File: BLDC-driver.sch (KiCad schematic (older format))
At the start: 9 parts, among them Q1 IPD50R380CE, Q2 IPD50R380CE, U1 NCP81151

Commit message: annotate
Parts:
- gave numbers to parts that had none: 5
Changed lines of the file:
@@
 	8650 3050 8650 2900
 $Comp
-L power:+5V #PWR?
+L power:+5V #PWR0104
 U 1 1 5EE8B1BC
 P 6850 1800
-F 0 "#PWR?" H 6850 1650 50  0001 C CNN
+F 0 "#PWR0104" H 6850 1650 50  0001 C CNN
 F 1 "+5V" H 6865 1973 50  0000 C CNN
 F 2 "" H 6850 1800 50  0001 C CNN
@@
 	6850 2000 7000 2000
 $Comp
-L Device:C_Small C?
+L Device:C_Small C2
 U 1 1 5EE8BA1A
 P 9000 1500
-F 0 "C?" H 9200 1550 50  0000 R CNN
+F 0 "C2" H 9200 1550 50  0000 R CNN
 F 1 "4.7uF" H 9200 1400 50  0000 R CNN
 F 2 "Capacitor_SMD:C_0603_1608Metric" H 9000 1500 50  0001 C CNN
@@
 $EndComp
 $Comp
-L power:GND #PWR?
+L power:GND #PWR0105
 U 1 1 5EE8C1E2
 P 9000 1600
-F 0 "#PWR?" H 9000 1350 50  0001 C CNN
+F 0 "#PWR0105" H 9000 1350 50  0001 C CNN
 F 1 "GND" H 9005 1427 50  0000 C CNN
 F 2 "" H 9000 1600 50  0001 C CNN
@@
 Connection ~ 8650 1400
 $Comp
-L Device:C_Small C?
+L Device:C_Small C3
 U 1 1 5EE8CF8E
 P 9200 1500
-F 0 "C?" H 9108 1546 50  0000 R CNN
+F 0 "C3" H 9108 1546 50  0000 R CNN
 F 1 "4.7uF" H 9108 1455 50  0000 R CNN
 F 2 "Capacitor_SMD:C_0603_1608Metric" H 9200 1500 50  0001 C CNN
@@
 $EndComp
 $Comp
-L power:GND #PWR?
+L power:GND #PWR0106
 U 1 1 5EE8D549
 P 9200 1600
-F 0 "#PWR?" H 9200 1350 50  0001 C CNN
+F 0 "#PWR0106" H 9200 1350 50  0001 C CNN
 F 1 "GND" H 9205 1427 50  0000 C CNN
 F 2 "" H 9200 1600 50  0001 C CNN
@@
 PH_A
 $Comp
-L Device:C_Small C?
+L Device:C_Small C4
 U 1 1 5EE8DE22
 P 6700 2000
-F 0 "C?" V 6800 2100 50  0000 R CNN
+F 0 "C4" V 6800 2100 50  0000 R CNN
 F 1 "4.7uF" V 6800 1950 50  0000 R CNN
 F 2 "Capacitor_SMD:C_0603_1608Metric" H 6700 2000 50  0001 C CNN
@@
 Connection ~ 6850 2000
 $Comp
-L power:GND #PWR?
+L power:GND #PWR0107
 U 1 1 5EE8F89C
 P 6550 2000
-F 0 "#PWR?" H 6550 1750 50  0001 C CNN
+F 0 "#PWR0107" H 6550 1750 50  0001 C CNN
 F 1 "GND" H 6555 1827 50  0000 C CNN
 F 2 "" H 6550 2000 50  0001 C CNN
@@
 	6550 2000 6600 2000
 $Comp
-L Transistor_FET:IPD50R380CE Q?
+L Transistor_FET:IPD50R380CE Q3
 U 1 1 5EE928AB
 P 9250 2100
-F 0 "Q?" H 9455 2131 50  0000 L CNN
+F 0 "Q3" H 9455 2131 50  0000 L CNN
 F 1 "IPD50R380CE" H 9455 2054 31  0000 L CNN
 F 2 "Package_TO_SOT_SMD:TO-252-2" H 9450 2025 50  0001 L CIN
@@
 Connection ~ 8350 2100
 $Comp
-L Transistor_FET:IPD50R380CE Q?
+L Transistor_FET:IPD50R380CE Q4
 U 1 1 5EE9355C
 P 9250 2700
-F 0 "Q?" H 9455 2731 50  0000 L CNN
+F 0 "Q4" H 9455 2731 50  0000 L CNN
 F 1 "IPD50R380CE" H 9455 2654 31  0000 L CNN
 F 2 "Package_TO_SOT_SMD:TO-252-2" H 9450 2625 50  0001 L CIN
@@
 Connection ~ 9350 2400
 $Comp
-L power:GND #PWR?
+L power:GND #PWR0108
 U 1 1 5EE9496B
 P 9350 3050
-F 0 "#PWR?" H 9350 2800 50  0001 C CNN
+F 0 "#PWR0108" H 9350 2800 50  0001 C CNN
 F 1 "GND" H 9355 2877 50  0000 C CNN
 F 2 "" H 9350 3050 50  0001 C CNN

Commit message: Schematic progress
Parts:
- removed Q1, Q2, Q3, Q4: IPD50R380CE, Package_TO_SOT_SMD:TO-252-2, symbol Transistor_FET:IPD50R380CE
- added C10, C6: 100nF, Capacitor_SMD:C_0603_1608Metric, symbol Device:C_Small
- added C11, C12, C5, C7, C8, C9: 4.7uF, Capacitor_SMD:C_0603_1608Metric, symbol Device:C_Small
- added Q1, Q2, Q3, Q4, Q5, Q6: FDMS86550, Package_TO_SOT_SMD:TDSON-8-1, symbol Transistor_FET:FDMS86550
- added U2, U3: NCP81151, Package_DFN_QFN:DFN-8-1EP_2x2mm_P0.5mm_EP0.9x1.3mm, symbol BLDC-driver-rescue:NCP81151-userdvc
- added U4: LPC1112FHN33-101, Package_DFN_QFN:QFN-32-1EP_7x7mm_P0.65mm_EP4.7x4.7mm, symbol MCU_NXP_LPC:LPC1112FHN33-101
- U1: symbol userdvc:NCP81151 -> BLDC-driver-rescue:NCP81151-userdvc
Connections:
- net labels added: +3.3V, HG_A, HG_B, HG_C, LG_A, LG_B, LG_C, PH_B, PH_C
- wire segments 35 -> 73
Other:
- moved on the sheet: C1, C2, C3, C4

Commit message: Latest
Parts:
- added C13, C14, C15: 2.7nF, Capacitor_SMD:C_0603_1608Metric, symbol Device:C_Small
- added C16, C17, C18: 4.7uF, Capacitor_SMD:C_1206_3216Metric, symbol Device:C_Small
- added R1, R2, R3: 2.2, Resistor_SMD:R_0603_1608Metric, symbol Device:R_Small
- added R4: 10k, Resistor_SMD:R_0603_1608Metric, symbol Device:R_Small
- added TH1: 10k, Resistor_SMD:R_0603_1608Metric, symbol Device:Thermistor_NTC
- added U5: AS5600, Package_SO:SOIC-8_3.9x4.9mm_P1.27mm, symbol BLDC-driver-rescue:AS5600
- C11, C12, C2, C3, C7, C8: footprint Capacitor_SMD:C_0603_1608Metric -> Capacitor_SMD:C_1206_3216Metric
- U1, U2, U3: footprint Package_DFN_QFN:DFN-8-1EP_2x2mm_P0.5mm_EP0.9x1.3mm -> Package_DFN_QFN:DFN-8-1EP_2x2mm_P0.5mm_EP0.9x1.5mm
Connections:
- net +24V: now also C16.1, C17.1, C18.1
- net +3V3: now also TH1.1
- net +5V: now also U1.3 (EN), U2.3 (EN), U3.3 (EN)
- net GND: now also C13.2, C14.2, C15.2, C16.2, C17.2, C18.2, R4.2, U5.4 (GND)
- net PH_A: now also R1.1
- net PH_B: now also R2.1
- net PH_C: now also R3.1
- net PWM_A: now reaches U1.2 (PWM)
- net PWM_A: now also U4.19 (PIO0_10)
- net PWM_B: now reaches U3.2 (PWM)
- net PWM_B: now also U4.21 (PIO0_11)
- net PWM_C: now reaches U2.2 (PWM)
- net PWM_C: now also U4.18 (PIO0_9)
- net ENBL: now reaches U4.17 (PIO0_8)
- new net: C13.1, R1.2
- new net: C14.1, R2.2
- new net: C15.1, R3.2
- new net FET_TEMP: R4.1, TH1.2

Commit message: Latest
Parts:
- added C19, C20: 100nF, Capacitor_SMD:C_0603_1608Metric, symbol Device:C_Small
- added J1: Conn_01x06, Connector_PinHeader_2.54mm:PinHeader_1x08_P2.54mm_Vertical, symbol Connector_Generic:Conn_01x08
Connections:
- net +3V3: now also U5.1 (VDD5V), U5.2 (VDD3V3), C20.2
- net FET_TEMP: now also U4.20 (PIO1_10), C19.2
- net GND: now also C19.1, C20.1, J1.1 (Pin_1)
- net PWM_A: now also U4.26 (PIO1_4); no longer U4.19 (PIO0_10)
- net PWM_B: now also U4.24 (PIO1_2); no longer U4.21 (PIO0_11)
- net PWM_C: now also U4.23 (PIO1_1); no longer U4.18 (PIO0_9)
- net SCL: now reaches U4.10 (PIO0_4)
- net SCL: now also U5.7 (SCL), J1.5 (Pin_5)
- net SDA: now reaches U4.11 (PIO0_5)
- net SDA: now also U5.6 (SDA), J1.6 (Pin_6)
- net SWDIO: now reaches U4.25 (PIO1_3)
- net SWDIO: now also J1.4 (Pin_4)
- net RXD: now reaches U4.31 (PIO1_6)
- net RXD: now also J1.8 (Pin_8)
- net TXD: now reaches U4.32 (PIO1_7)
- net TXD: now also J1.7 (Pin_7)
- net ENBL: no longer names the net of U4.17 (PIO0_8)
- new net SWCLK: J1.3 (Pin_3), U4.19 (PIO0_10)
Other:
- note added: "CT32B1_MAT0"
- note added: "CT32B1_MAT1"
- note added: "CT32B1_MAT3"
- moved on the sheet: U5
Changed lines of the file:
@@
 P 3300 3150
 F 0 "U4" H 3300 3000 50  0000 C CNN
-F 1 "LPC1112FHN33-101" H 3200 2650 50  0000 C CNN
+F 1 "LPC1112FHN33-101" H 3150 2700 50  0000 C CNN
 F 2 "Package_DFN_QFN:QFN-32-1EP_7x7mm_P0.65mm_EP4.7x4.7mm" H 4400 4250 50  0001 C CNN
 F 3 "https://www.nxp.com/documents/data_sheet/LPC111X.pdf" H 3300 3150 50  0001 C CNN
@@
 L BLDC-driver-rescue:AS5600 U5
 U 1 1 5EFF18B3
-P 5450 3200
-F 0 "U5" H 5625 3365 50  0000 C CNN
-F 1 "AS5600" H 5625 3274 50  0000 C CNN
-F 2 "Package_SO:SOIC-8_3.9x4.9mm_P1.27mm" H 5450 3200 50  0001 C CNN
-F 3 "" H 5450 3200 50  0001 C CNN
-	1    5450 3200
+P 6250 3250
+F 0 "U5" H 6425 3415 50  0000 C CNN
+F 1 "AS5600" H 6425 3324 50  0000 C CNN
+F 2 "Package_SO:SOIC-8_3.9x4.9mm_P1.27mm" H 6250 3250 50  0001 C CNN
+F 3 "" H 6250 3250 50  0001 C CNN
+	1    6250 3250
 	1    0    0    -1
 $EndComp
@@
 L power:GND #PWR0130
 U 1 1 5EFF1DB5
-P 5100 3600
-F 0 "#PWR0130" H 5100 3350 50  0001 C CNN
-F 1 "GND" H 5105 3427 50  0000 C CNN
-F 2 "" H 5100 3600 50  0001 C CNN
-F 3 "" H 5100 3600 50  0001 C CNN
-	1    5100 3600
-	1    0    0    -1
-$EndComp
-Text Label 2600 3250 2    50   ~ 0
+P 5900 3650
+F 0 "#PWR0130" H 5900 3400 50  0001 C CNN
+F 1 "GND" H 5905 3477 50  0000 C CNN
+F 2 "" H 5900 3650 50  0001 C CNN
+F 3 "" H 5900 3650 50  0001 C CNN
+	1    5900 3650
+	1    0    0    -1
+$EndComp
+Text Label 4200 2450 0    50   ~ 0
 PWM_C
-Text Label 2600 3350 2    50   ~ 0
+Text Label 4200 2750 0    50   ~ 0
 PWM_A
-Text Label 2600 3450 2    50   ~ 0
+Text Label 4200 2550 0    50   ~ 0
 PWM_B
-Text Label 2600 3150 2    50   ~ 0
-ENBL
 $Comp
 L power:+5V #PWR0131
@@
 L power:GND #PWR0134
 U 1 1 5F0691FC
-P 5900 1900
-F 0 "#PWR0134" H 5900 1650 50  0001 C CNN
-F 1 "GND" H 5905 1727 50  0000 C CNN
-F 2 "" H 5900 1900 50  0001 C CNN
-F 3 "" H 5900 1900 50  0001 C CNN
-	1    5900 1900
+P 5900 2000
+F 0 "#PWR0134" H 5900 1750 50  0001 C CNN
+F 1 "GND" H 5905 1827 50  0000 C CNN
+F 2 "" H 5900 2000 50  0001 C CNN
+F 3 "" H 5900 2000 50  0001 C CNN
+	1    5900 2000
 	1    0    0    -1
 $EndComp
@@
 	1    0    0    -1
 $EndComp
-Text Label 6100 1600 0    50   ~ 0
+Text Label 6650 1600 0    50   ~ 0
 FET_TEMP
-Wire Wire Line
-	6100 1600 5900 1600
 Connection ~ 5900 1600
 Wire Wire Line
 	5900 1600 5900 1500
+Text Label 2400 2750 2    50   ~ 0
+SCL
+Text Label 2400 2850 2    50   ~ 0
+SDA
+Wire Wire Line
+	2400 2850 2600 2850
+Wire Wire Line
+	2600 2750 2400 2750
+Text Label 2400 3350 2    50   ~ 0
+SWCLK
+Text Label 4200 2650 0    50   ~ 0
+SWDIO
+Wire Wire Line
+	4200 2650 4000 2650
+Wire Wire Line
+	2600 3350 2400 3350
+Text Label 4200 2950 0    50   ~ 0
+RXD
+Text Label 4200 3050 0    50   ~ 0
+TXD
+Wire Wire Line
+	4200 3050 4000 3050
+Wire Wire Line
+	4000 2950 4200 2950
+Wire Wire Line
+	4200 2450 4000 2450
+Wire Wire Line
+	4000 2550 4200 2550
+Wire Wire Line
+	4000 2750 4200 2750
+Text Notes 4550 2750 0    50   ~ 0
+CT32B1_MAT3
+Text Notes 4550 2550 0    50   ~ 0
+CT32B1_MAT1
+Text Notes 4550 2450 0    50   ~ 0
+CT32B1_MAT0
+$Comp
+L power:+3.3V #PWR0136
+U 1 1 5F0C7A64
+P 5700 3250
+F 0 "#PWR0136" H 5700 3100 50  0001 C CNN
+F 1 "+3.3V" H 5715 3423 50  0000 C CNN
+F 2 "" H 5700 3250 50  0001 C CNN
+F 3 "" H 5700 3250 50  0001 C CNN
+	1    5700 3250
+	1    0    0    -1
+$EndComp
+Wire Wire Line
+	5700 3250 5700 3350
+Wire Wire Line
+	5700 3450 5900 3450
+Wire Wire Line
+	5900 3350 5700 3350
+Connection ~ 5700 3350
+Wire Wire Line
+	5700 3350 5700 3450
+$Comp
+L Device:C_Small C20
+U 1 1 5F0CF40D
+P 5500 3550
+F 0 "C20" V 5271 3550 50  0000 C CNN
+F 1 "100nF" V 5362 3550 50  0000 C CNN
+F 2 "Capacitor_SMD:C_0603_1608Metric" H 5500 3550 50  0001 C CNN
+F 3 "~" H 5500 3550 50  0001 C CNN
+	1    5500 3550
+	-1   0    0    1
+$EndComp
+Wire Wire Line
+	5500 3450 5700 3450
+Connection ~ 5700 3450
+Wire Wire Line
+	5500 3650 5900 3650
+Connection ~ 5900 3650
+Text Label 7150 3450 0    50   ~ 0
+SCL
+Text Label 7150 3550 0    50   ~ 0
+SDA
+Wire Wire Line
+	7150 3550 6950 3550
+Wire Wire Line
+	6950 3450 7150 3450
+$Comp
+L Device:C_Small C19
+U 1 1 5F0DE4B5
+P 6250 1750
+F 0 "C19" V 6021 1750 50  0000 C CNN
+F 1 "100nF" V 6112 1750 50  0000 C CNN
+F 2 "Capacitor_SMD:C_0603_1608Metric" H 6250 1750 50  0001 C CNN
+F 3 "~" H 6250 1750 50  0001 C CNN
+	1    6250 1750
+	-1   0    0    1
+$EndComp
+Wire Wire Line
+	5900 1600 6250 1600
+Wire Wire Line
+	6250 1650 6250 1600
+Connection ~ 6250 1600
+Wire Wire Line
+	6250 1600 6650 1600
+Wire Wire Line
+	5900 2000 5900 1950
+Wire Wire Line
+	5900 1950 6250 1950
+Wire Wire Line
+	6250 1950 6250 1850
+Connection ~ 5900 1950
+Wire Wire Line
+	5900 1950 5900 1900
+Text Label 4200 3350 0    50   ~ 0
+FET_TEMP
+Wire Wire Line
+	4000 3350 4200 3350
+$Comp
+L Connector_Generic:Conn_01x08 J1
+U 1 1 5F108F52
+P 1250 5800
+F 0 "J1" H 1168 5175 50  0000 C CNN
+F 1 "Conn_01x06" H 1168 5266 50  0000 C CNN
+F 2 "Connector_PinHeader_2.54mm:PinHeader_1x08_P2.54mm_Vertical" H 1250 5800 50  0001 C CNN
+F 3 "~" H 1250 5800 50  0001 C CNN
+	1    1250 5800
+	-1   0    0    1
+$EndComp
+Text Label 1650 5400 0    50   ~ 0
+RXD
+Text Label 1650 5500 0    50   ~ 0
+TXD
+Wire Wire Line
+	1650 5500 1450 5500
+Wire Wire Line
+	1450 5400 1650 5400
+Text Label 1650 5700 0    50   ~ 0
+SCL
+Text Label 1650 5600 0    50   ~ 0
+SDA
+Wire Wire Line
+	1650 5600 1450 5600
+Wire Wire Line
+	1450 5700 1650 5700
+Text Label 1650 5900 0    50   ~ 0
+SWCLK
+Text Label 1650 5800 0    50   ~ 0
+SWDIO
+Wire Wire Line
+	1650 5800 1450 5800
+Wire Wire Line
+	1450 5900 1650 5900
+$Comp
+L power:GND #PWR0137
+U 1 1 5F120A4B
+P 1450 6100
+F 0 "#PWR0137" H 1450 5850 50  0001 C CNN
+F 1 "GND" H 1455 5927 50  0000 C CNN
+F 2 "" H 1450 6100 50  0001 C CNN
+F 3 "" H 1450 6100 50  0001 C CNN
+	1    1450 6100
+	1    0    0    -1
+$EndComp
 $EndSCHEMATC

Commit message: Latest
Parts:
- added C23: 10nF, Capacitor_SMD:C_0603_1608Metric, symbol Device:C_Small
- added C24, C25, C26: 1uF, Capacitor_SMD:C_0603_1608Metric, symbol Device:C_Small
- added C5, C6: 100nF, Capacitor_SMD:C_0603_1608Metric, symbol Device:C_Small
- added D1: 30V, Diode_SMD:D_SOD-323, symbol Device:D_Schottky_Small
- added JP1: BOOT, Jumper:SolderJumper-2_P1.3mm_Open_Pad1.0x1.5mm, symbol Device:Jumper
- added L1: 4.7uH, Inductor_SMD:L_Taiyo-Yuden_MD-3030, symbol Device:L_Small
- added NT1: Net-Tie_2, NetTie:NetTie-2_SMD_Pad0.5mm, symbol Device:Net-Tie_2
- added R2, R3: 10k, Resistor_SMD:R_0603_1608Metric, symbol Device:R_Small
- added R7: 100k, Resistor_SMD:R_0603_1608Metric, symbol Device:R_Small
- added R8: 47k, Resistor_SMD:R_0603_1608Metric, symbol Device:R_Small
- added R9: 9.1k, Resistor_SMD:R_0603_1608Metric, symbol Device:R_Small
- added U6: MP2359, Package_TO_SOT_SMD:SOT-23-6, symbol BLDC-driver-rescue:MP2359
- added U7: MIC5504-3.3YM5, Package_TO_SOT_SMD:SOT-23-5, symbol Regulator_Linear:MIC5504-3.3YM5
- J1: footprint Connector_PinHeader_2.54mm:PinHeader_1x08_P2.54mm_Vertical -> Connector_PinHeader_2.00mm:PinHeader_1x08_P2.00mm_Vertical
- U1: value NCP81151 -> ADP3120A
- U4: renamed from U3; value NCP81151 -> ADP3120A
- U5: renamed from U2; value NCP81151 -> ADP3120A
- renumbered C2 to C1, C7 to C10, C8 to C11, C17 to C12, C10 to C13, C9 to C14, C11 to C15, C12 to C16, C18 to C17, C6 to C18, C5 to C19, C3 to C2, C13 to C20, C14 to C21, C15 to C22, C16 to C3, C19 to C4, C1 to C7, C4 to C8, C20 to C9, TH1 to NTC1, Q3 to Q1, Q4 to Q2, Q5 to Q3, Q6 to Q4, Q1 to Q5, Q2 to Q6, R4 to R1, R1 to R4, R2 to R5, R3 to R6, U4 to U2, U5 to U3
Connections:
- net +24V: now also R7.1, U6.5 (IN)
- net +3V3: now also R1.1, C25.2, C5.2, C6.2, R2.1, R3.1, U7.5 (VOUT); no longer NTC1.1
- net +5V: now also J1.2 (Pin_2), C24.2, C26.2, L1.2, R8.2, U7.1 (VIN), U7.3 (EN)
- net FET_TEMP: now also NTC1.1, R1.2, U2.30 (PIO1_5); no longer NTC1.2, R1.1, U2.20 (PIO1_10)
- net GND: now also C24.1, C25.1, C26.1, C5.1, C6.1, D1.2 (A), JP1.1, NT1.1, R9.1, U6.2 (GND), U7.2 (GND); no longer C1.2, C10.2, C11.2, C12.2, C14.2, C15.2, C16.2, C17.2, C19.2, C2.2, C20.2, C21.2, C22.2, C3.2, C8.2, Q2.1 (S), Q2.2 (S), Q2.3 (S), Q4.1 (S), Q4.2 (S), Q4.3 (S), Q6.1 (S), Q6.2 (S), Q6.3 (S), R1.2, U1.6 (GND), U1.9 (PAD), U4.6 (GND), U4.9 (PAD), U5.6 (GND), U5.9 (PAD)
- net SCL: now also J1.6 (Pin_6), R2.2; no longer J1.5 (Pin_5)
- net SDA: now also J1.5 (Pin_5), R3.2; no longer J1.6 (Pin_6)
- net SWCLK: now also J1.4 (Pin_4); no longer J1.3 (Pin_3)
- net SWDIO: now also J1.3 (Pin_3); no longer J1.4 (Pin_4)
- net BOOT: now reaches U2.3 (PIO0_1)
- net BOOT: now also JP1.2
- new net: C23.2, U6.1 (BST)
- new net: R8.1, R9.2, U6.3 (FB)
- new net: R7.2, U6.4 (EN)
- new net: C23.1, D1.1 (K), L1.1, U6.6 (SW)
- new net GNDPWR: C1.2, C10.2, C11.2, C12.2, C14.2, C15.2, C16.2, C17.2, C19.2, C2.2, C20.2, C21.2, C22.2, C3.2, C8.2, NT1.2, NTC1.2, Q2.1 (S), Q2.2 (S), Q2.3 (S), Q4.1 (S), Q4.2 (S), Q4.3 (S), Q6.1 (S), Q6.2 (S), Q6.3 (S), U1.6 (GND), U1.9 (PAD), U4.6 (GND), U4.9 (PAD), U5.6 (GND), U5.9 (PAD)
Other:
- note added: "AD6"
- moved on the sheet: NTC1, R1

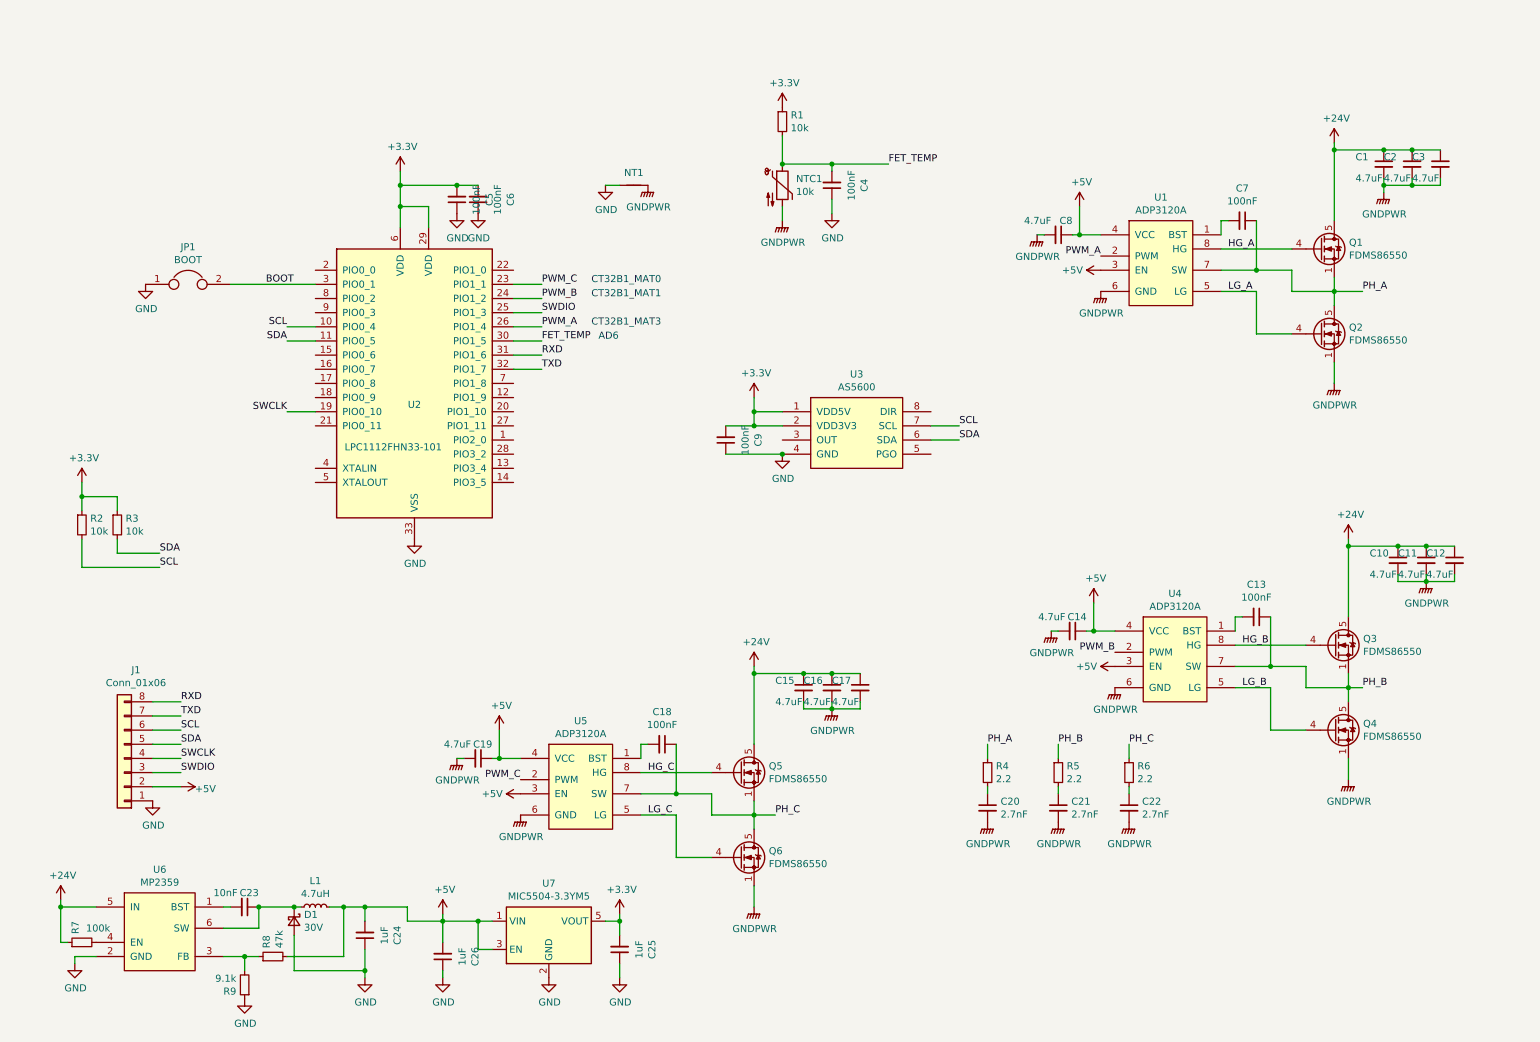
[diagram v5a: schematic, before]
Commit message: Change to stm32f103c8t6
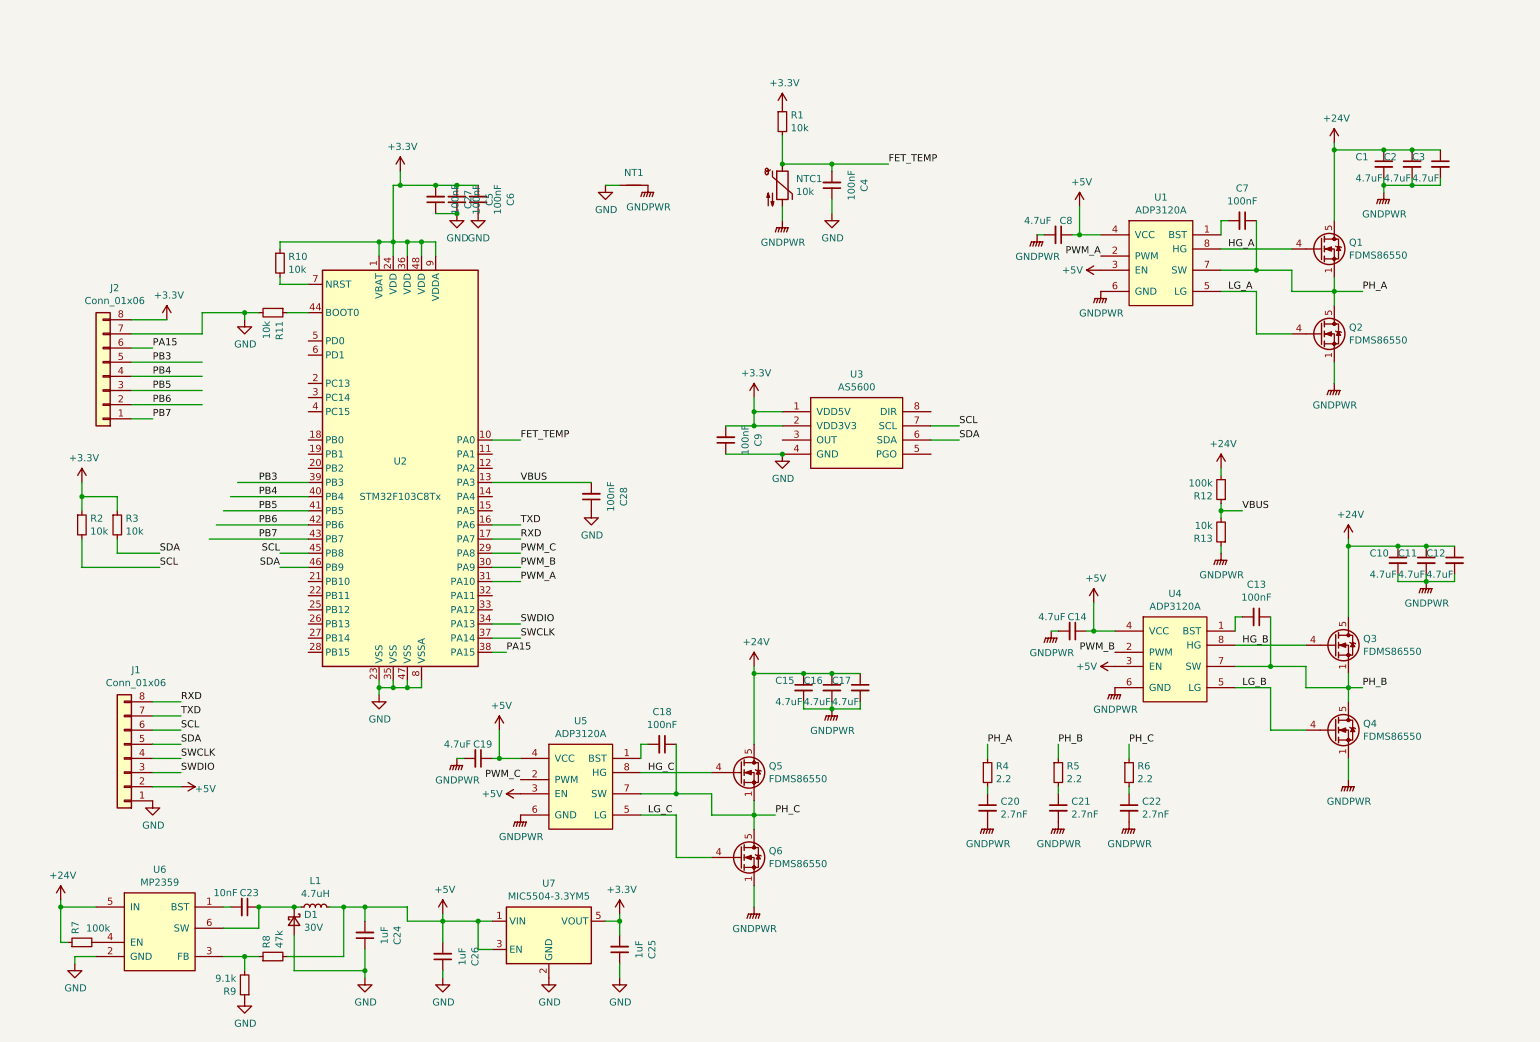
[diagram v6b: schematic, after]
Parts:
- removed JP1: BOOT, Jumper:SolderJumper-2_P1.3mm_Open_Pad1.0x1.5mm, symbol Device:Jumper
- removed U2: LPC1112FHN33-101, Package_DFN_QFN:QFN-32-1EP_7x7mm_P0.65mm_EP4.7x4.7mm, symbol MCU_NXP_LPC:LPC1112FHN33-101
- added C27, C28: 100nF, Capacitor_SMD:C_0603_1608Metric, symbol Device:C_Small
- added J2: Conn_01x06, Connector_PinHeader_2.00mm:PinHeader_1x08_P2.00mm_Vertical, symbol Connector_Generic:Conn_01x08
- added R10, R11, R13: 10k, Resistor_SMD:R_0603_1608Metric, symbol Device:R_Small
- added R12: 100k, Resistor_SMD:R_0603_1608Metric, symbol Device:R_Small
- added U2: STM32F103C8Tx, Package_QFP:LQFP-48_7x7mm_P0.5mm, symbol MCU_ST_STM32F1:STM32F103C8Tx
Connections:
- net labels added: PA15, PB3, PB4, PB5, PB6, PB7, VBUS
- net labels removed: BOOT
- wire segments 179 -> 224
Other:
- note removed: "AD6"
- note removed: "CT32B1_MAT0"
- note removed: "CT32B1_MAT1"
- note removed: "CT32B1_MAT3"
